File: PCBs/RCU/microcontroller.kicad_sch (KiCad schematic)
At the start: 23 parts, among them J200 USB_C_Receptacle_USB2.0, J201 Conn_01x05, SW201 SW_Push, U200 STM32G0B1CBT6, Y200 16MHz

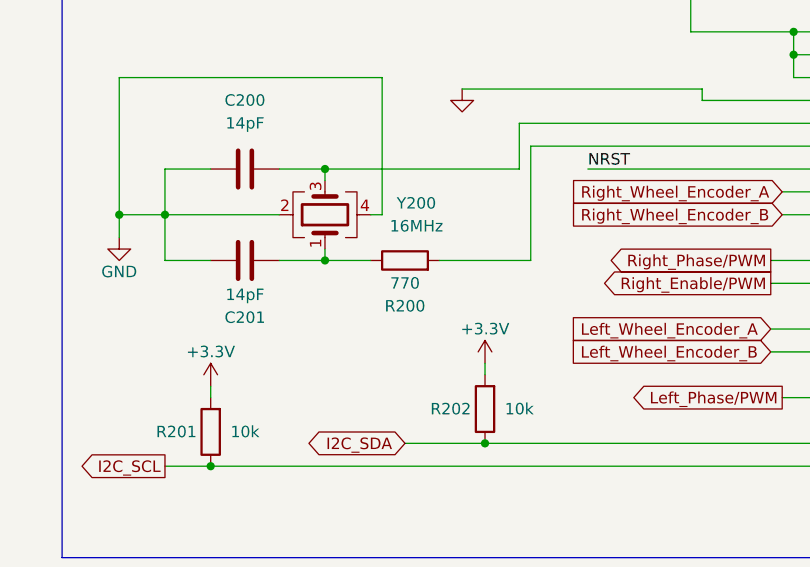
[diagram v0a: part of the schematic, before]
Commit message: Use Rext = 0 ohms for oscillator circuit
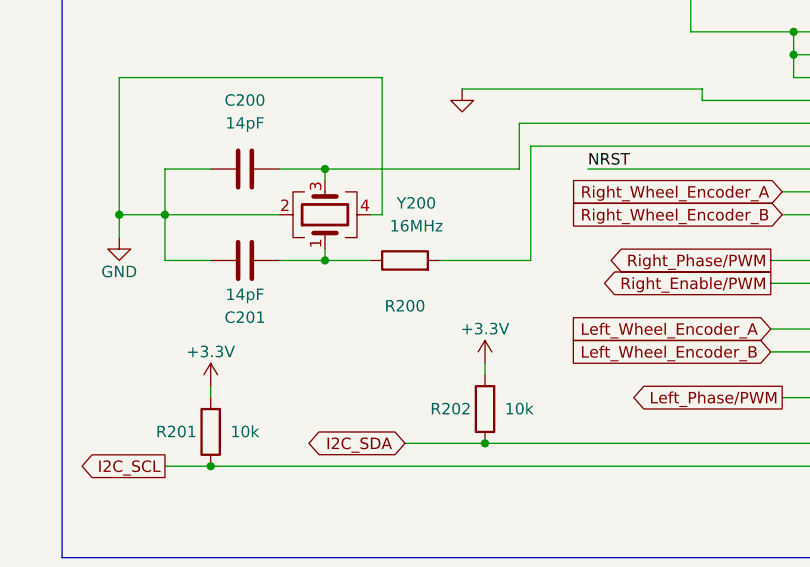
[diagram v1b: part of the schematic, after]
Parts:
- R200: value 770 -> (none)
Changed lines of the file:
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@@
     (in_bom yes) (on_board yes)
     (property "Reference" "R200" (id 0) (at 91.44 83.82 90))
-    (property "Value" "770" (id 1) (at 91.44 81.28 90))
+    (property "Value" "" (id 1) (at 91.44 81.28 90))
     (property "Footprint" "" (id 2) (at 91.44 80.518 90)
       (effects (font (size 1.27 1.27)) hide)

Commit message: Corrected cap values in regulators, changed voltage after battery filter to 9V, will use a 6V regulator to power motors in the near future
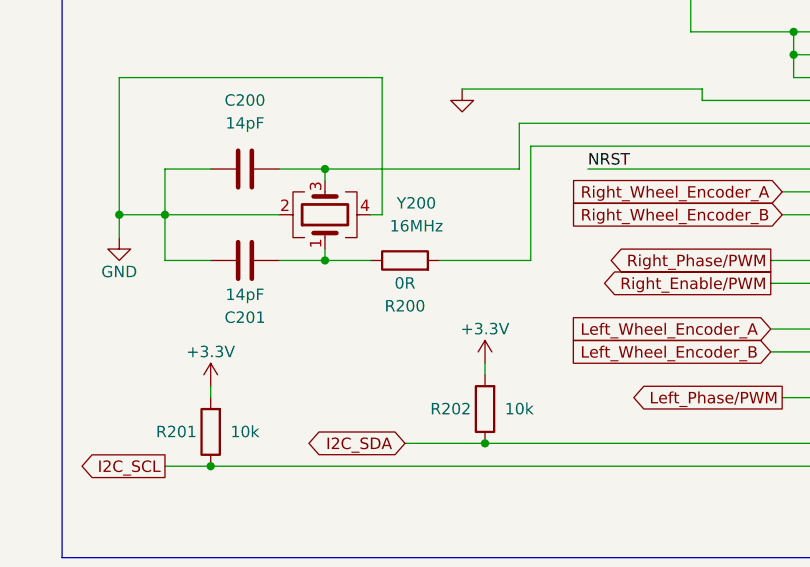
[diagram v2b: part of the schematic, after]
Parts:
- R200: value (none) -> 0R
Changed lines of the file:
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@@
     (in_bom yes) (on_board yes)
     (property "Reference" "R200" (id 0) (at 91.44 83.82 90))
-    (property "Value" "" (id 1) (at 91.44 81.28 90))
+    (property "Value" "0R" (id 1) (at 91.44 81.28 90))
     (property "Footprint" "" (id 2) (at 91.44 80.518 90)
       (effects (font (size 1.27 1.27)) hide)

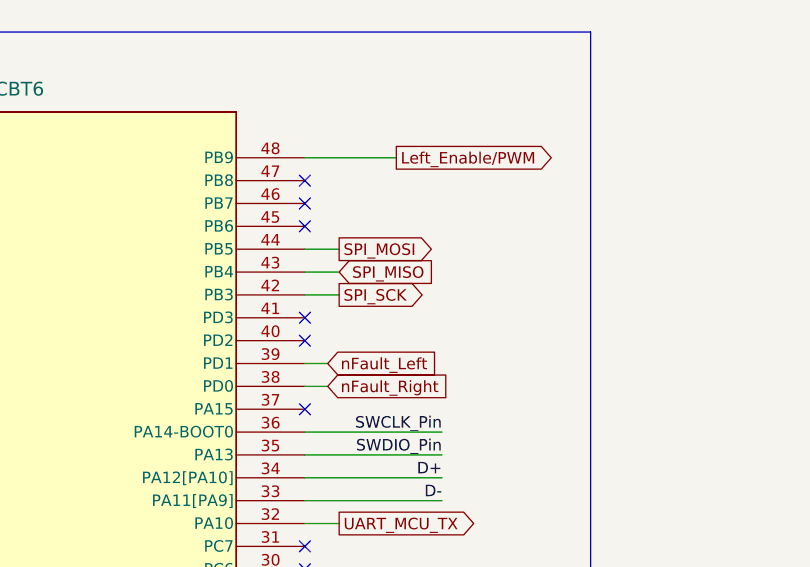
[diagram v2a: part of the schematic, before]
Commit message: Added 32Mbit external memory with SPI interface
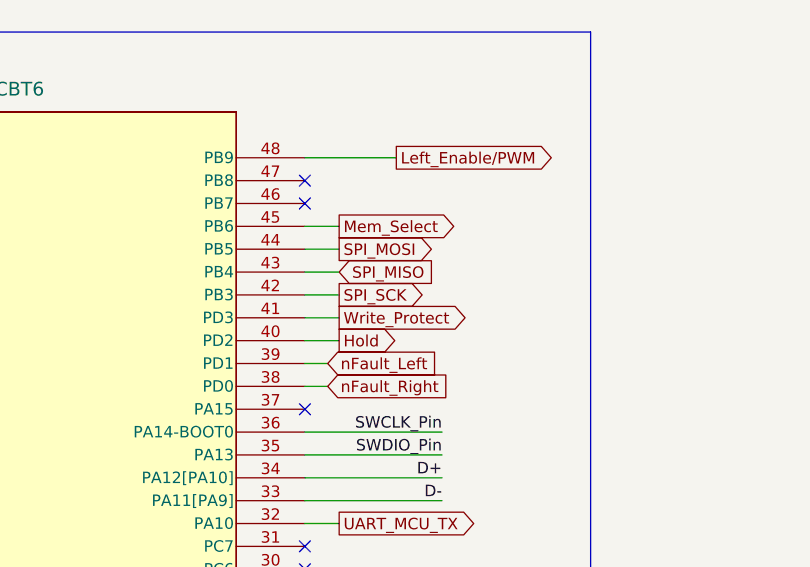
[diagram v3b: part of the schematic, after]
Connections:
- net Hold: now reaches U200.40 (PD2)
- net Write_Protect: now reaches U200.41 (PD3)
- net Mem_Select: now reaches U200.45 (PB6)
- no-connect marks 20 -> 17
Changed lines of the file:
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@@
   )
   (no_connect (at 76.2 168.91))
-  (no_connect (at 213.36 66.04))
   (no_connect (at 137.16 76.2))
   (no_connect (at 137.16 83.82))
@@
   (no_connect (at 213.36 48.26))
   (no_connect (at 213.36 50.8))
-  (no_connect (at 213.36 53.34))
   (no_connect (at 213.36 96.52))
   (no_connect (at 213.36 99.06))
-  (no_connect (at 213.36 63.5))
   (no_connect (at 76.2 171.45))
   (wire (pts (xy 76.2 140.97) (xy 81.28 140.97))
@@
     (stroke (width 0) (type default) (color 0 0 0 0))
   )
+  (wire (pts (xy 217.17 53.34) (xy 213.36 53.34))
+    (stroke (width 0) (type default) (color 0 0 0 0))
+  )
   (wire (pts (xy 95.25 78.74) (xy 105.41 78.74))
     (stroke (width 0) (type default) (color 0 0 0 0))
@@
     (stroke (width 0) (type default) (color 0 0 0 0))
   )
+  (wire (pts (xy 217.17 63.5) (xy 213.36 63.5))
+    (stroke (width 0) (type default) (color 0 0 0 0))
+  )
   (wire (pts (xy 182.88 124.46) (xy 176.53 124.46))
     (stroke (width 0) (type default) (color 0 0 0 0))
@@
   )
   (wire (pts (xy 213.36 81.28) (xy 228.6 81.28))
+    (stroke (width 0) (type default) (color 0 0 0 0))
+  )
+  (wire (pts (xy 217.17 66.04) (xy 213.36 66.04))
     (stroke (width 0) (type default) (color 0 0 0 0))
   )
@@
     )
   )
+  (global_label "Hold" (shape output) (at 217.17 66.04 0) (fields_autoplaced)
+    (effects (font (size 1.27 1.27)) (justify left))
+    (property "Intersheet References" "${INTERSHEET_REFS}" (id 0) (at 223.8769 65.9606 0)
+      (effects (font (size 1.27 1.27)) (justify left) hide)
+    )
+  )
   (global_label "nFault_Right" (shape input) (at 215.9 71.12 0) (fields_autoplaced)
     (effects (font (size 1.27 1.27)) (justify left))
@@
     )
   )
+  (global_label "Write_Protect" (shape output) (at 217.17 63.5 0) (fields_autoplaced)
+    (effects (font (size 1.27 1.27)) (justify left))
+    (property "Intersheet References" "${INTERSHEET_REFS}" (id 0) (at 232.0412 63.4206 0)
+      (effects (font (size 1.27 1.27)) (justify left) hide)
+    )
+  )
+  (global_label "Mem_Select" (shape output) (at 217.17 53.34 0) (fields_autoplaced)
+    (effects (font (size 1.27 1.27)) (justify left))
+    (property "Intersheet References" "${INTERSHEET_REFS}" (id 0) (at 230.6502 53.2606 0)
+      (effects (font (size 1.27 1.27)) (justify left) hide)
+    )
+  )

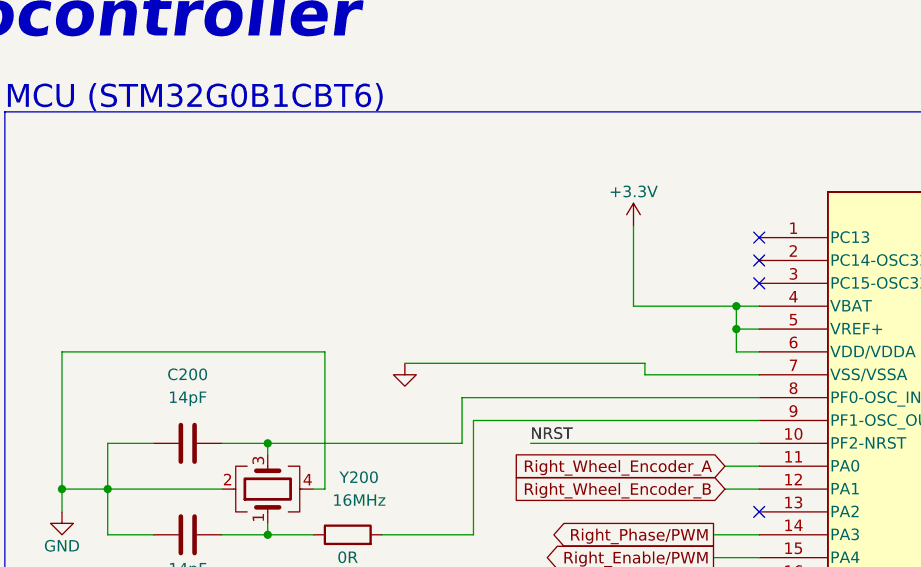
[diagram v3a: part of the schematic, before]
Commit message: Add filtering capacitors to microcontroller circuit
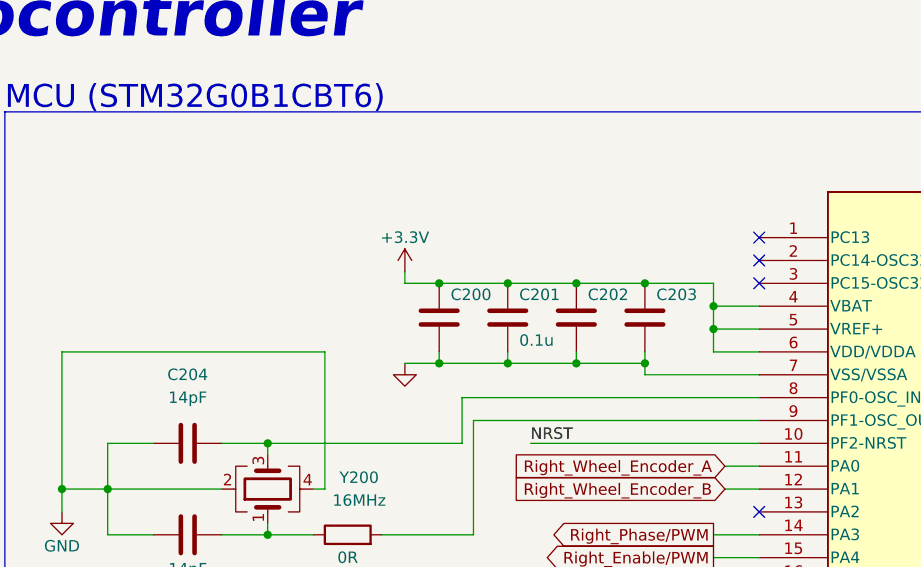
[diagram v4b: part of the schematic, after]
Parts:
- added C200, C202, C203: (no value), symbol Device:C
- added C201: 0.1u, symbol Device:C
- renumbered C200 to C204
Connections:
- net +3V3: now also C200.1, C201.1, C202.1, C203.1
- net GND: now also C200.2, C201.2, C202.2, C203.2

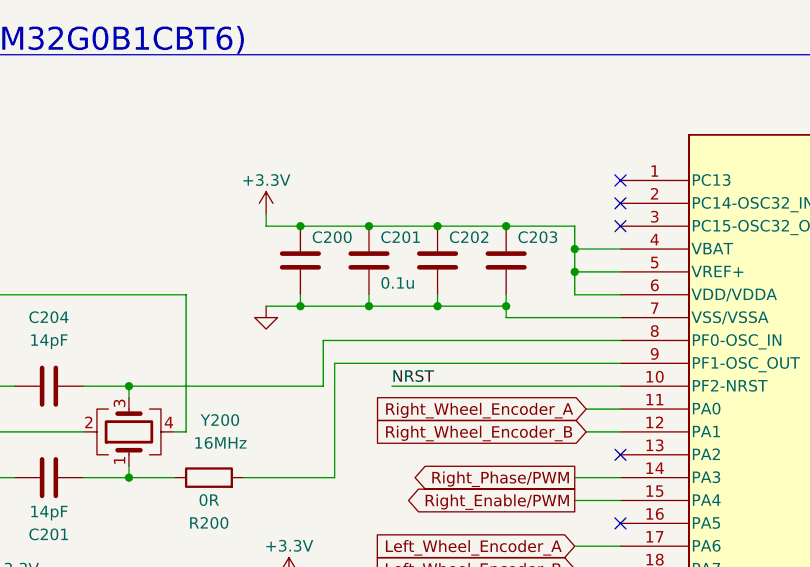
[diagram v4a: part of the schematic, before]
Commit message: scaled down encoder output from 6V to 4V
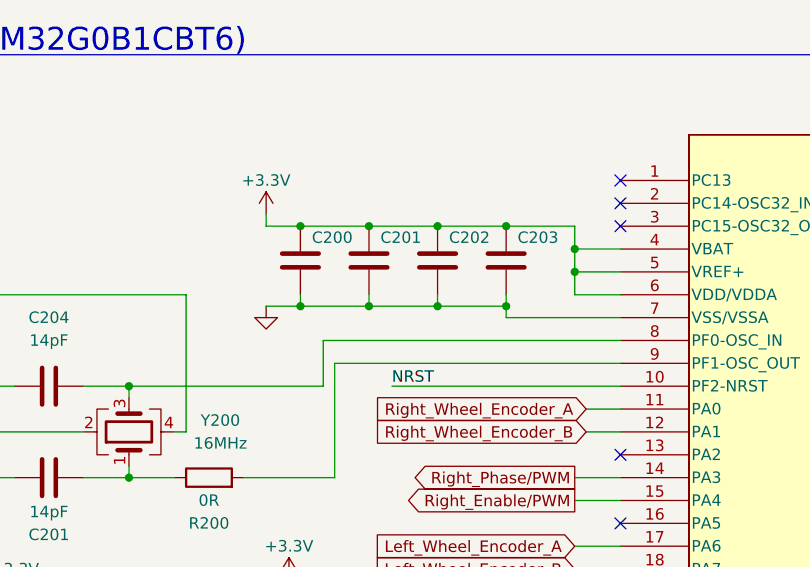
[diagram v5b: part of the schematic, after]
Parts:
- C201: value 0.1u -> (none)
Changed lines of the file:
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@@
       (effects (font (size 1.27 1.27)) (justify left))
     )
-    (property "Value" "0.1u" (id 1) (at 110.49 57.15 0)
+    (property "Value" "" (id 1) (at 110.49 57.15 0)
       (effects (font (size 1.27 1.27)) (justify left))
     )

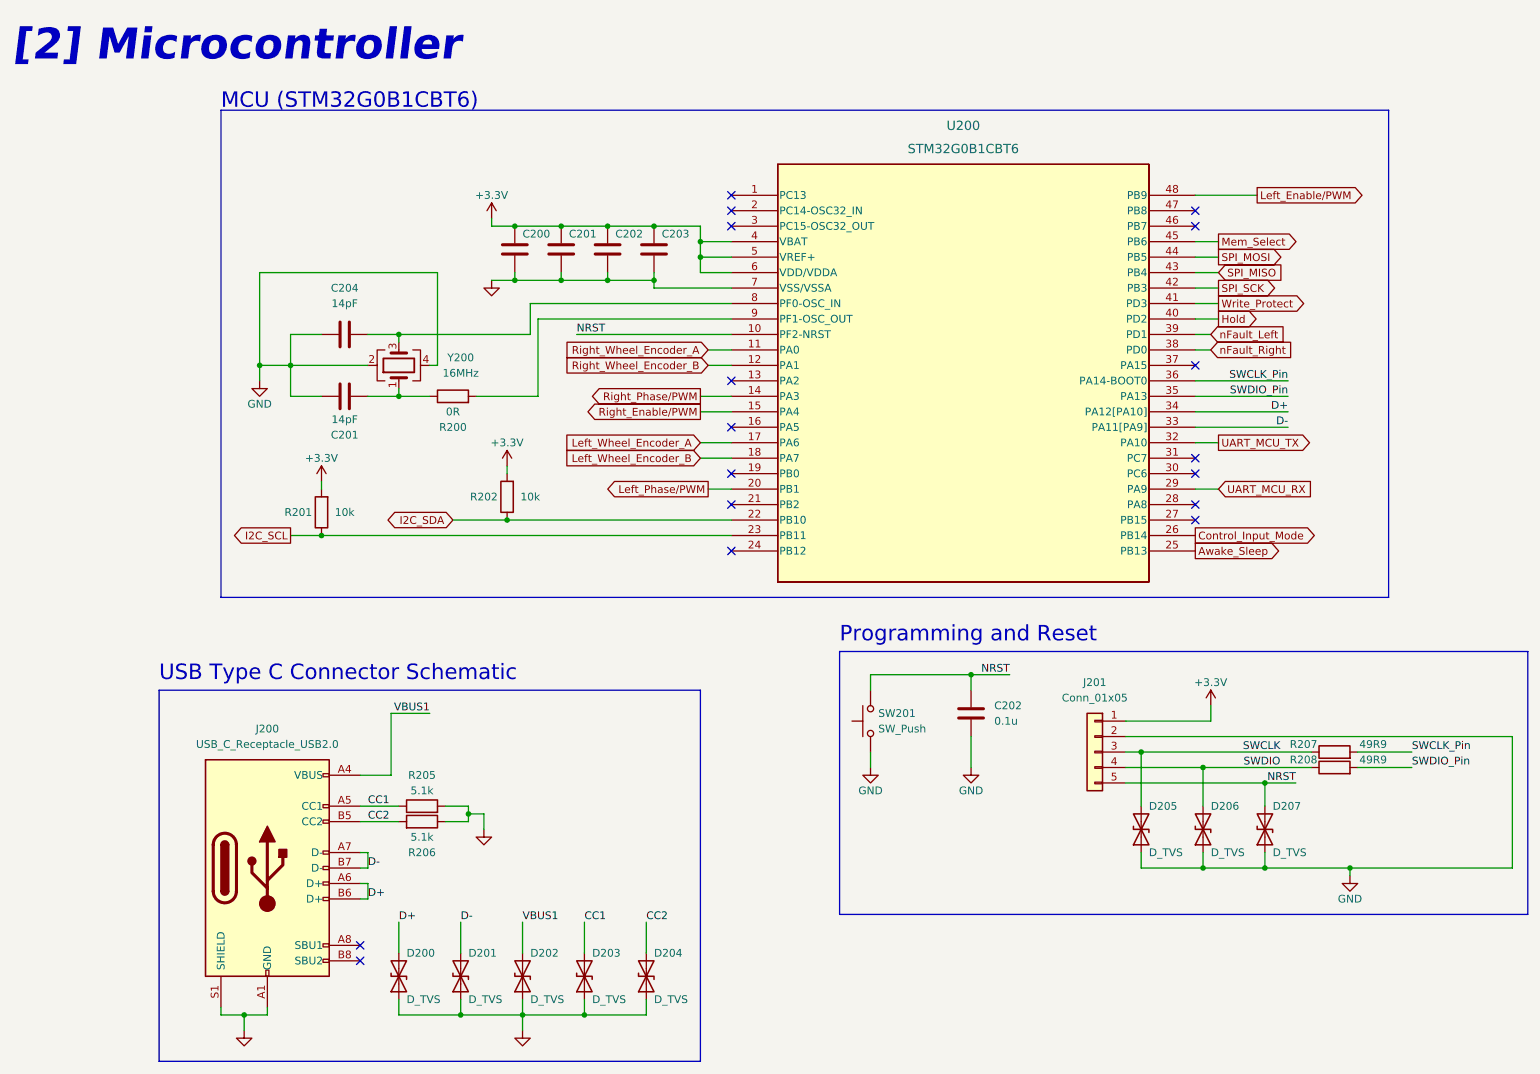
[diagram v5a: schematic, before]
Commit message: Replaced Bidrectional TVS diodes with USBLC-2SC6 unidirectional ESD protection
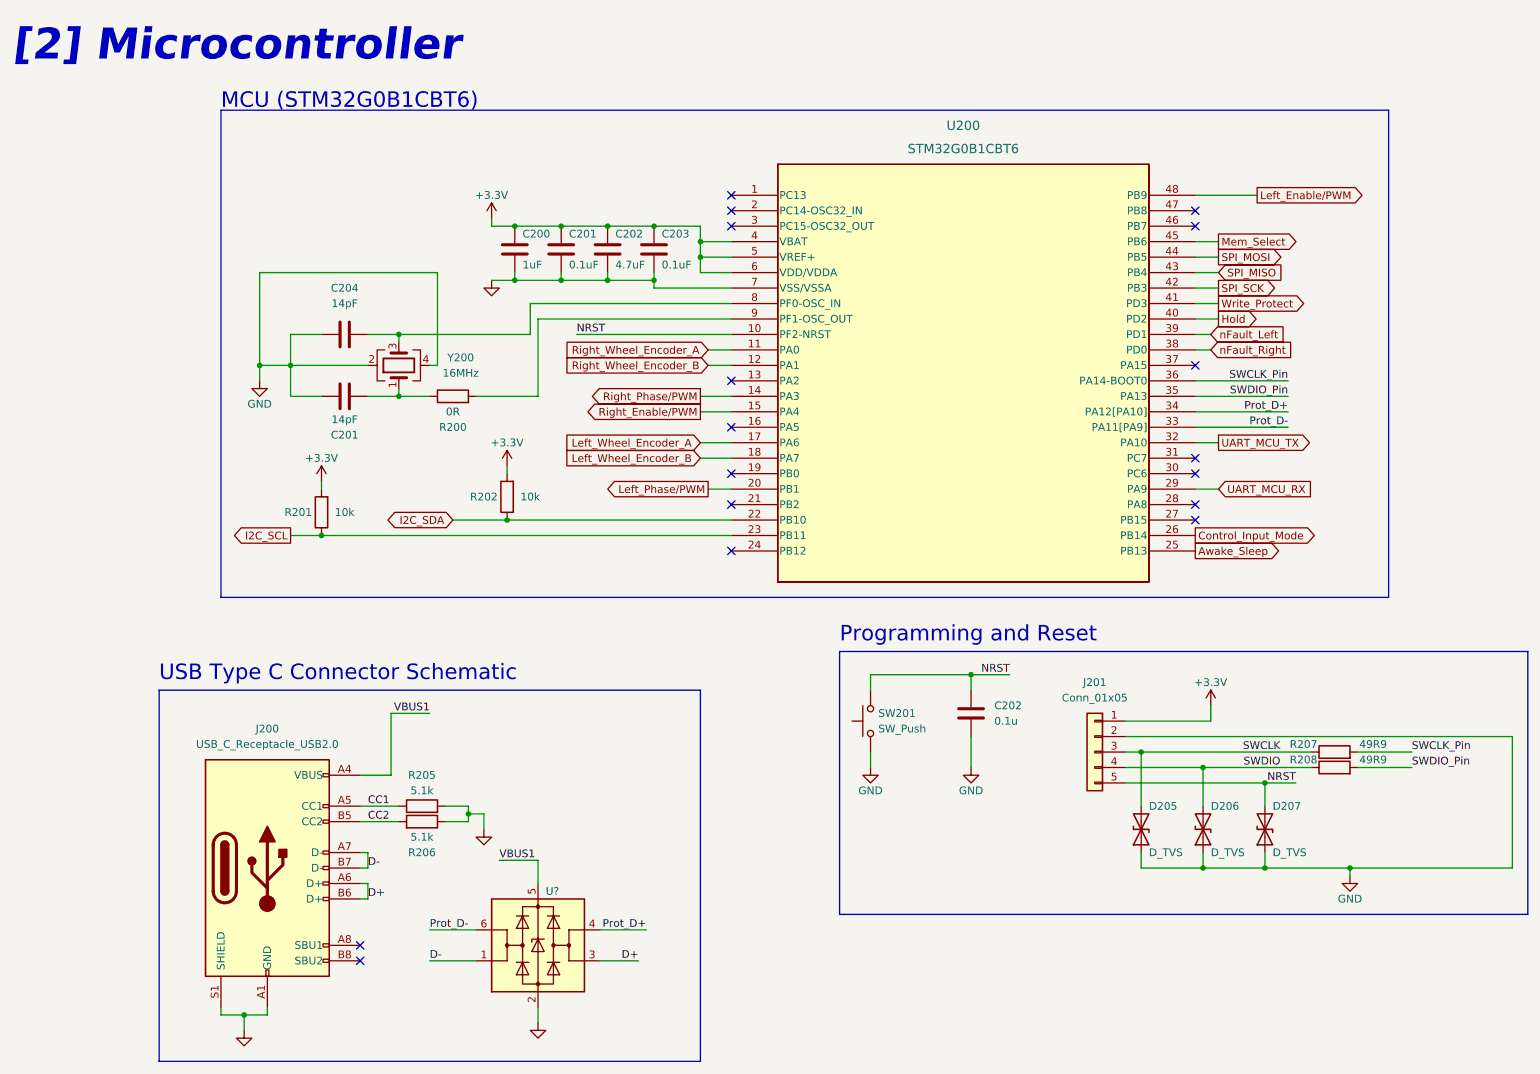
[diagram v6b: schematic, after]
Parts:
- removed D200, D201, D202, D203, D204: D_TVS, symbol Device:D_TVS
- added U?: (no value), symbol Power_Protection:USBLC6-2SC6
- C200: value (none) -> 1uF
- C201, C203: value (none) -> 0.1uF
- C202: value (none) -> 4.7uF
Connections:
- net D+: now also U?.3 (I/O2); no longer U200.34 (PA12[PA10])
- net D-: now also U?.1 (I/O1); no longer U200.33 (PA11[PA9])
- net GND: now also U?.2 (GND)
- net VBUS1: now also U?.5 (VBUS)
- new net Prot_D+: U200.34 (PA12[PA10]), U?.4 (I/O2)
- new net Prot_D-: U200.33 (PA11[PA9]), U?.6 (I/O1)
